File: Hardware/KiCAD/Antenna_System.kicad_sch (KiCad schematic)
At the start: 23 parts, among them IC1 GRF5504, IC3 GRF5504, IC4 BQ24193RGER, IC5 BQ24193RGER, J2 Conn_Coaxial_UHF

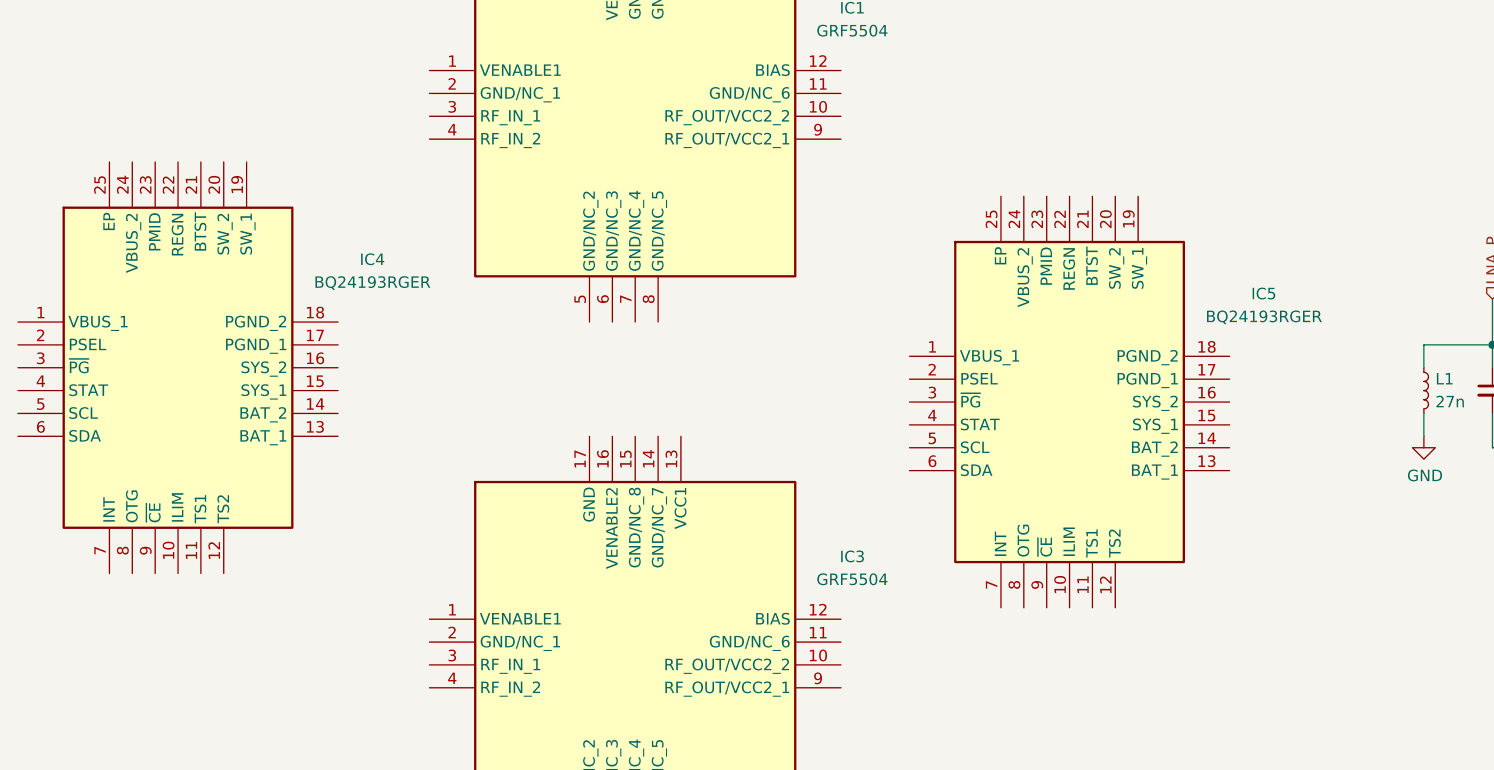
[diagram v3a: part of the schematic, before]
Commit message: Changed Keypad to better accomidate use of GPIO and removed inc symbols
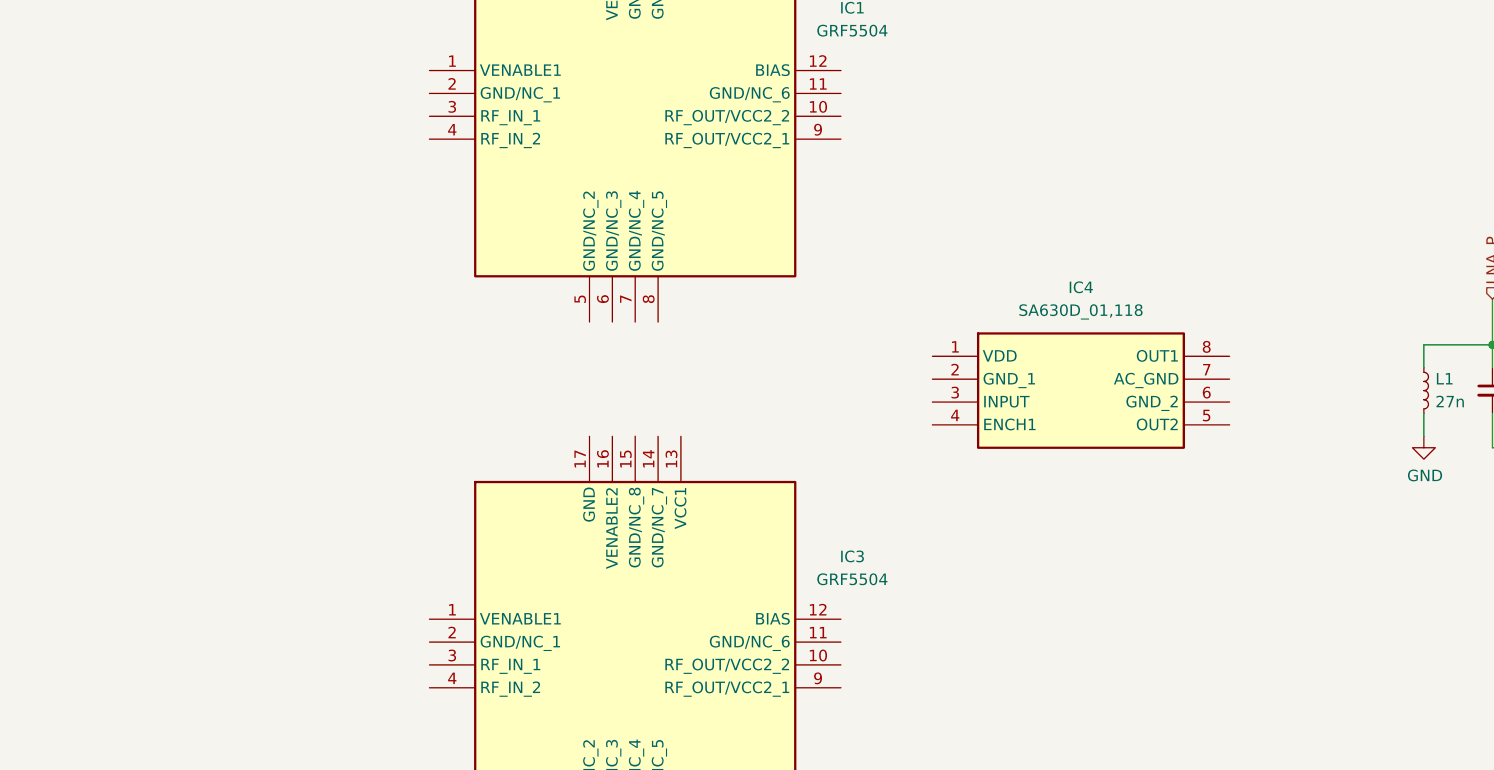
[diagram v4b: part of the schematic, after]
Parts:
- removed IC4, IC5: BQ24193RGER, Cobalt_Cowboy:QFN50P400X400X100-25N-D_BQ24193RGER, symbol Cobalt-Cowboy:BQ24193RGER
- added IC4: SA630D_01,118, Cobalt_Cowboy:SOIC127P600X175-8N_SA630D_01,118, symbol Cobalt-Cowboy:SA630D_01,118
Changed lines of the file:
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@@
-    )
-  )
-  (symbol (lib_id "Cobalt-Cowboy:BQ24193RGER") (at 17.78 90.17 0) (unit 1)
-    (in_bom yes) (on_board yes) (dnp no) (fields_autoplaced)
-    (property "Reference" "IC4" (at 57.15 83.2419 0)
-      (effects (font (size 1.27 1.27)))
-    )
-    (property "Value" "BQ24193RGER" (at 57.15 85.7819 0)
-      (effects (font (size 1.27 1.27)))
-    )
-    (property "Footprint" "Cobalt_Cowboy:QFN50P400X400X100-25N-D_BQ24193RGER" (at 49.53 174.93 0)
-      (effects (font (size 1.27 1.27)) (justify left top) hide)
-    )
-    (property "Datasheet" "http://www.ti.com/lit/gpn/bq24193" (at 49.53 274.93 0)
-      (effects (font (size 1.27 1.27)) (justify left top) hide)
-    )
-    (property "Height" "1" (at 49.53 474.93 0)
-      (effects (font (size 1.27 1.27)) (justify left top) hide)
-    )
-    (property "Manufacturer_Name" "Texas Instruments" (at 49.53 574.93 0)
-      (effects (font (size 1.27 1.27)) (justify left top) hide)
-    )
-    (property "Manufacturer_Part_Number" "BQ24193RGER" (at 49.53 674.93 0)
-      (effects (font (size 1.27 1.27)) (justify left top) hide)
-    )
-    (property "Mouser Part Number" "595-BQ24193RGER" (at 49.53 774.93 0)
-      (effects (font (size 1.27 1.27)) (justify left top) hide)
-    )
-    (property "Mouser Price/Stock" "https://www.mouser.co.uk/ProductDetail/Texas-Instruments/BQ24193RGER?qs=E2%2FxqS9xjzprfPaRl%2FdVSQ%3D%3D" (at 49.53 874.93 0)
-      (effects (font (size 1.27 1.27)) (justify left top) hide)
-    )
-    (property "Arrow Part Number" "BQ24193RGER" (at 49.53 974.93 0)
-      (effects (font (size 1.27 1.27)) (justify left top) hide)
-    )
-    (property "Arrow Price/Stock" "https://www.arrow.com/en/products/bq24193rger/texas-instruments" (at 49.53 1074.93 0)
-      (effects (font (size 1.27 1.27)) (justify left top) hide)
-    )
-    (pin "19")
-    (pin "16")
-    (pin "10")
-    (pin "6")
-    (pin "2")
-    (pin "25")
-    (pin "15")
-    (pin "1")
-    (pin "4")
-    (pin "21")
-    (pin "8")
-    (pin "5")
-    (pin "18")
-    (pin "11")
-    (pin "20")
-    (pin "3")
-    (pin "14")
-    (pin "13")
-    (pin "23")
-    (pin "22")
-    (pin "7")
-    (pin "17")
-    (pin "9")
-    (pin "12")
-    (pin "24")
-    (instances
-      (project "Cobalt-Cowboy"
-        (path "/60a68eb1-aa0f-414e-b03b-965ad6b52dab/2f7042f8-0d23-4099-8d81-3056d19c4a6f"
-          (reference "IC4") (unit 1)
-        )
-      )
     )
   )
@@
     )
   )
-  (symbol (lib_id "Cobalt-Cowboy:BQ24193RGER") (at 116.84 93.98 0) (unit 1)
-    (in_bom yes) (on_board yes) (dnp no) (fields_autoplaced)
-    (property "Reference" "IC5" (at 156.21 87.0519 0)
-      (effects (font (size 1.27 1.27)))
-    )
-    (property "Value" "BQ24193RGER" (at 156.21 89.5919 0)
-      (effects (font (size 1.27 1.27)))
-    )
-    (property "Footprint" "Cobalt_Cowboy:QFN50P400X400X100-25N-D_BQ24193RGER" (at 148.59 178.74 0)
-      (effects (font (size 1.27 1.27)) (justify left top) hide)
-    )
-    (property "Datasheet" "http://www.ti.com/lit/gpn/bq24193" (at 148.59 278.74 0)
-      (effects (font (size 1.27 1.27)) (justify left top) hide)
-    )
-    (property "Height" "1" (at 148.59 478.74 0)
-      (effects (font (size 1.27 1.27)) (justify left top) hide)
-    )
-    (property "Manufacturer_Name" "Texas Instruments" (at 148.59 578.74 0)
-      (effects (font (size 1.27 1.27)) (justify left top) hide)
-    )
-    (property "Manufacturer_Part_Number" "BQ24193RGER" (at 148.59 678.74 0)
-      (effects (font (size 1.27 1.27)) (justify left top) hide)
-    )
-    (property "Mouser Part Number" "595-BQ24193RGER" (at 148.59 778.74 0)
-      (effects (font (size 1.27 1.27)) (justify left top) hide)
-    )
-    (property "Mouser Price/Stock" "https://www.mouser.co.uk/ProductDetail/Texas-Instruments/BQ24193RGER?qs=E2%2FxqS9xjzprfPaRl%2FdVSQ%3D%3D" (at 148.59 878.74 0)
-      (effects (font (size 1.27 1.27)) (justify left top) hide)
-    )
-    (property "Arrow Part Number" "BQ24193RGER" (at 148.59 978.74 0)
-      (effects (font (size 1.27 1.27)) (justify left top) hide)
-    )
-    (property "Arrow Price/Stock" "https://www.arrow.com/en/products/bq24193rger/texas-instruments" (at 148.59 1078.74 0)
-      (effects (font (size 1.27 1.27)) (justify left top) hide)
-    )
-    (pin "19")
-    (pin "16")
-    (pin "10")
+  (symbol (lib_id "Cobalt-Cowboy:SA630D_01,118") (at 119.38 93.98 0) (unit 1)
+    (in_bom yes) (on_board yes) (dnp no) (fields_autoplaced)
+    (property "Reference" "IC4" (at 135.89 86.36 0)
+      (effects (font (size 1.27 1.27)))
+    )
+    (property "Value" "SA630D_01,118" (at 135.89 88.9 0)
+      (effects (font (size 1.27 1.27)))
+    )
+    (property "Footprint" "Cobalt_Cowboy:SOIC127P600X175-8N_SA630D_01,118" (at 148.59 188.9 0)
+      (effects (font (size 1.27 1.27)) (justify left top) hide)
+    )
+    (property "Datasheet" "http://www.nxp.com/docs/en/data-sheet/SA630.pdf" (at 148.59 288.9 0)
+      (effects (font (size 1.27 1.27)) (justify left top) hide)
+    )
+    (property "Height" "1.75" (at 148.59 488.9 0)
+      (effects (font (size 1.27 1.27)) (justify left top) hide)
+    )
+    (property "Manufacturer_Name" "NXP" (at 148.59 588.9 0)
+      (effects (font (size 1.27 1.27)) (justify left top) hide)
+    )
+    (property "Manufacturer_Part_Number" "SA630D/01,118" (at 148.59 688.9 0)
+      (effects (font (size 1.27 1.27)) (justify left top) hide)
+    )
+    (property "Mouser Part Number" "771-SA630D/01-T" (at 148.59 788.9 0)
+      (effects (font (size 1.27 1.27)) (justify left top) hide)
+    )
+    (property "Mouser Price/Stock" "https://www.mouser.co.uk/ProductDetail/NXP-Semiconductors/SA630D-01118?qs=LOCUfHb8d9u4rxNYFnxIPQ%3D%3D" (at 148.59 888.9 0)
+      (effects (font (size 1.27 1.27)) (justify left top) hide)
+    )
+    (property "Arrow Part Number" "SA630D/01,118" (at 148.59 988.9 0)
+      (effects (font (size 1.27 1.27)) (justify left top) hide)
+    )
+    (property "Arrow Price/Stock" "https://www.arrow.com/en/products/sa630d01118/nxp-semiconductors?region=nac" (at 148.59 1088.9 0)
+      (effects (font (size 1.27 1.27)) (justify left top) hide)
+    )
+    (pin "3")
+    (pin "2")
     (pin "6")
-    (pin "2")
-    (pin "25")
-    (pin "15")
-    (pin "1")
+    (pin "1")
+    (pin "5")
     (pin "4")
-    (pin "21")
+    (pin "7")
     (pin "8")
-    (pin "5")
-    (pin "18")
-    (pin "11")
-    (pin "20")
-    (pin "3")
-    (pin "14")
-    (pin "13")
-    (pin "23")
-    (pin "22")
-    (pin "7")
-    (pin "17")
-    (pin "9")
-    (pin "12")
-    (pin "24")
-    (instances
-      (project "Cobalt-Cowboy"
-        (path "/60a68eb1-aa0f-414e-b03b-965ad6b52dab/2f7042f8-0d23-4099-8d81-3056d19c4a6f"
-          (reference "IC5") (unit 1)
-        )
-      )
+    (instances
+      (project "Cobalt-Cowboy"
+        (path "/60a68eb1-aa0f-414e-b03b-965ad6b52dab/2f7042f8-0d23-4099-8d81-3056d19c4a6f"
+          (reference "IC4") (unit 1)
+        )
+      )

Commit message: Added seperate schematic for amplifier assembly
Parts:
- removed IC1, IC3: GRF5504, Cobalt_Cowboy:QFN50P300X300X90-17N_GRF5504, symbol Cobalt-Cowboy:GRF5504
- removed IC4: SA630D_01,118, Cobalt_Cowboy:SOIC127P600X175-8N_SA630D_01,118, symbol Cobalt-Cowboy:SA630D_01,118
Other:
- added sheet Amplifier_Assembly (Amplifier_Assembly.kicad_sch)
- note added: "What Voltage is VDD?"
- moved on the sheet: C17, C18, C19, C20, C21, C22, C23, C24, C25, J2, L1, L2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

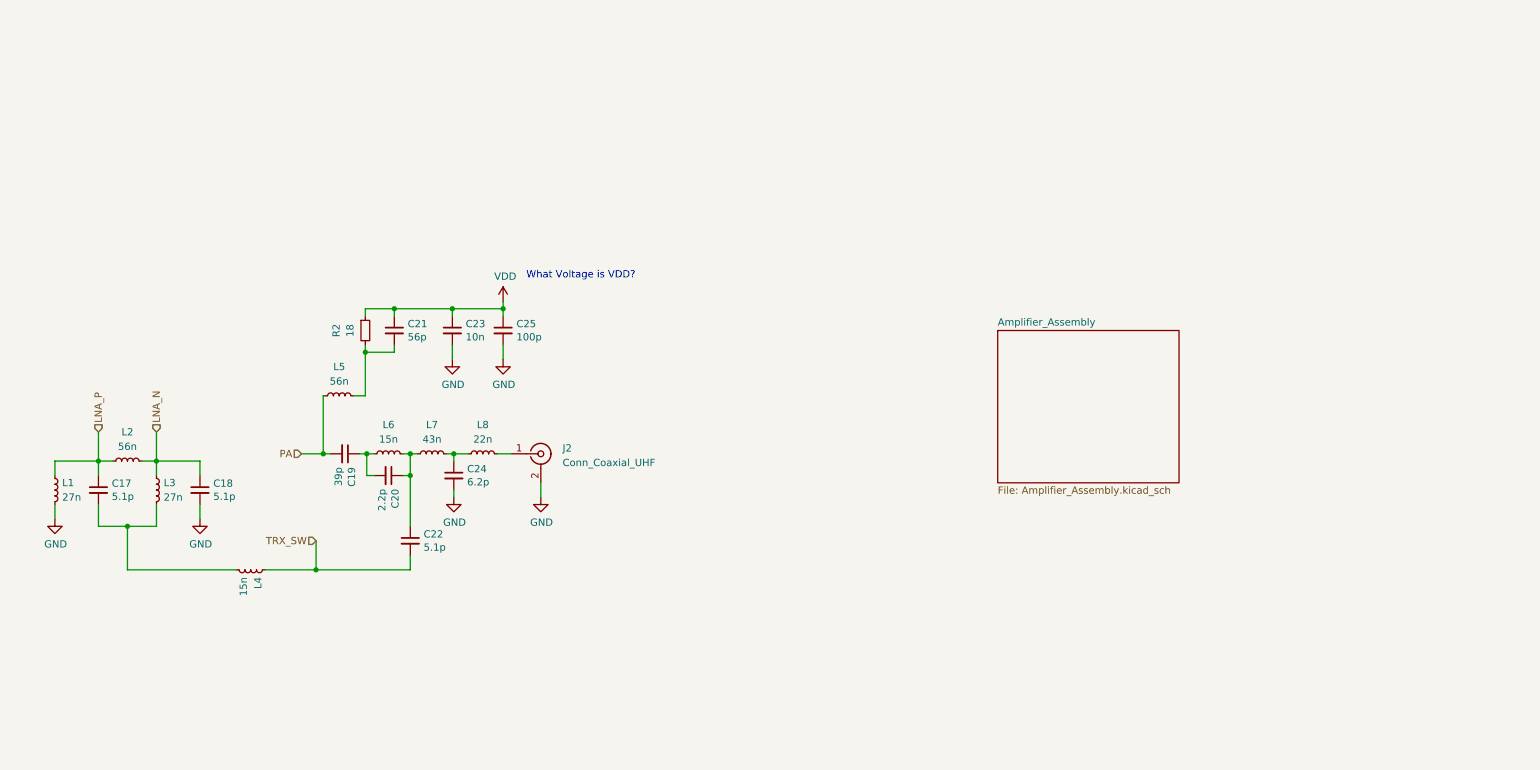
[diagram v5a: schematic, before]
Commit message: Added biasing, Still need to add actual values
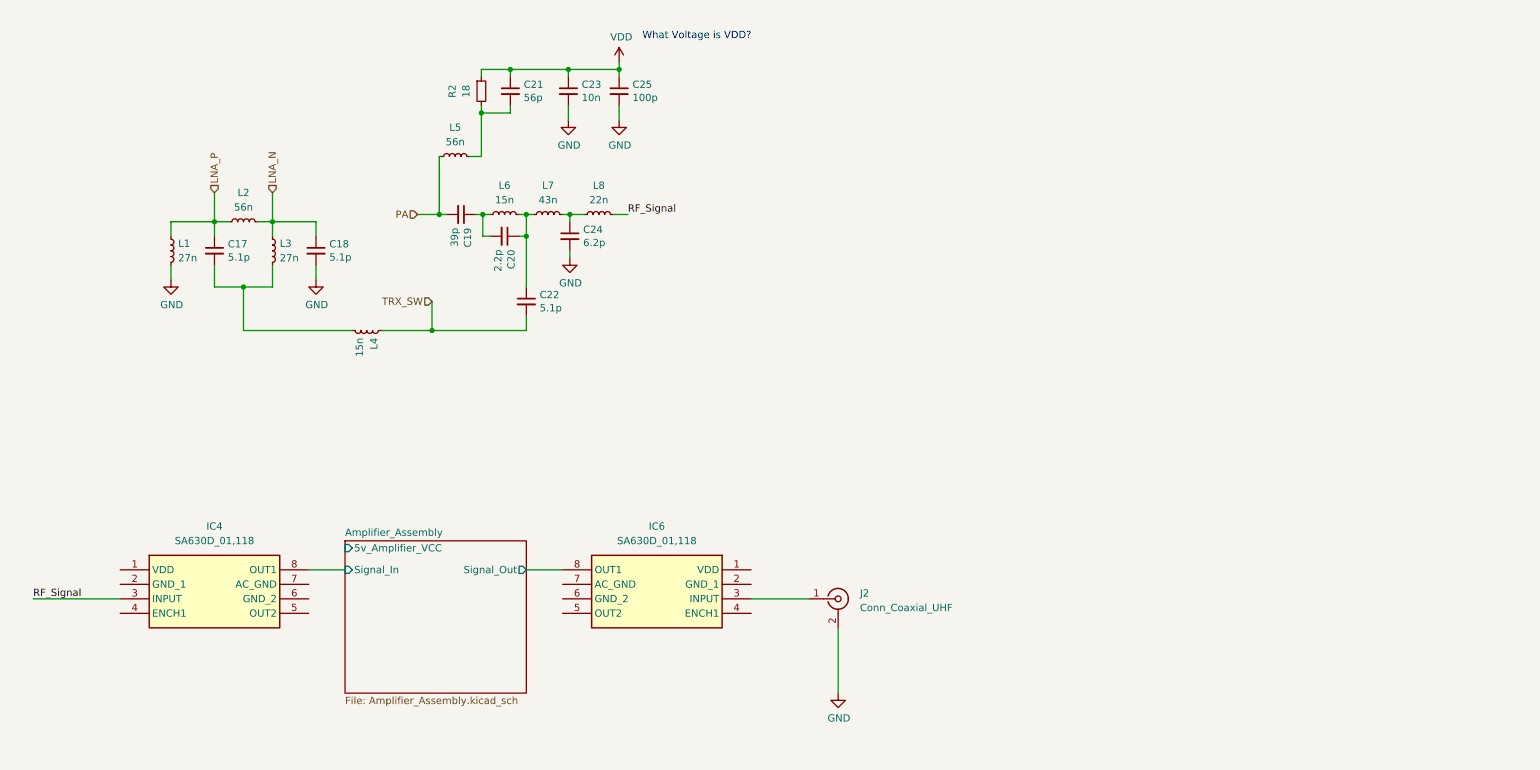
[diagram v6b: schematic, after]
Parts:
- added IC4, IC6: SA630D_01,118, Cobalt_Cowboy:SOIC127P600X175-8N_SA630D_01,118, symbol Cobalt-Cowboy:SA630D_01,118
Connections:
- net at J2.1 (In): now also IC6.3 (INPUT); no longer L8.2
- new net Amplifier_Assembly/Signal_In: IC4.8 (OUT1)
- new net Amplifier_Assembly/Signal_Out: IC6.8 (OUT1)
- new net RF_Signal: IC4.3 (INPUT), L8.2
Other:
- sheet Amplifier_Assembly ports: added 5v_Amplifier_VCC, Signal_In, Signal_Out; removed none
- moved on the sheet: C17, C18, C19, C20, C21, C22, C23, C24, C25, J2, L1, L2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
